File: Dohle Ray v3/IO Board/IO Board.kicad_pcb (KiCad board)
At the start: 2 copper layers, 50 x 41 mm, 5 parts, among them J1 Conn_01x07_Female, SW1 SW_SPDT

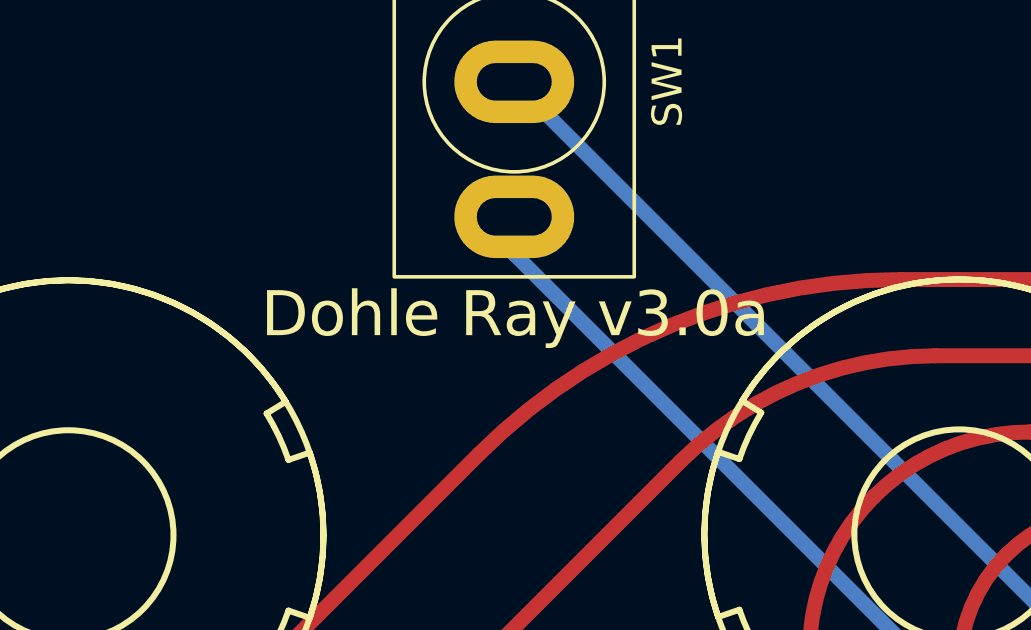
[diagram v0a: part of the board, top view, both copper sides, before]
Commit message: Update resistor values to have unity gain at 0% volume and gain knob, update PCB revision
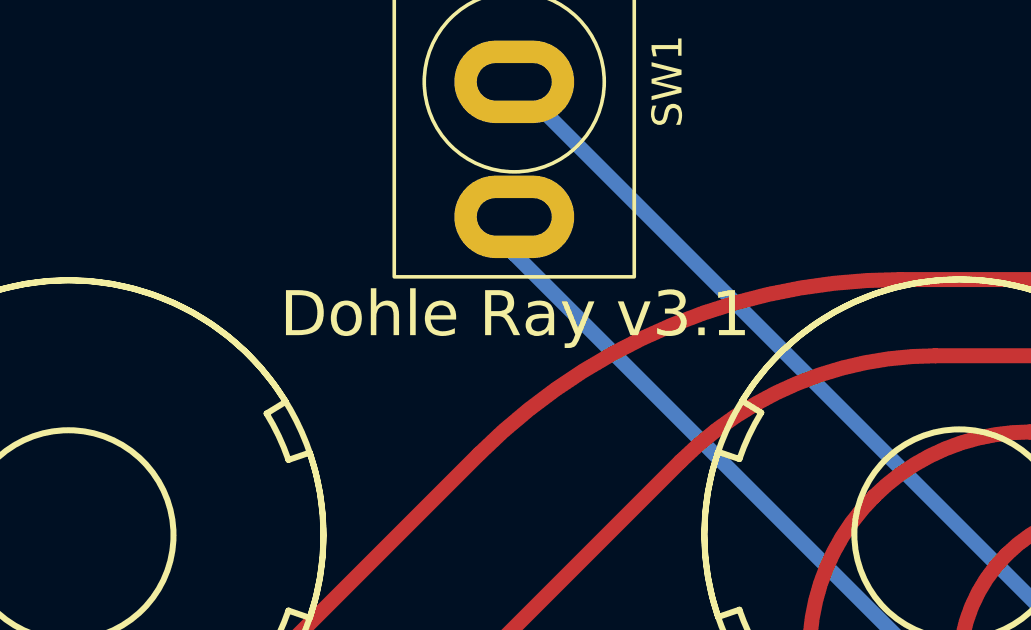
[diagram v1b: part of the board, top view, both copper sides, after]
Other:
- board text added: "Dohle Ray v3.1"
- board text removed: "Dohle Ray v3.0a"
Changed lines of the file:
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@@
   (gr_line (start 164.223286 135.963496) (end 164.223286 98.963496) (layer "Edge.Cuts") (width 0.2))
   (gr_line (start 162.223286 96.963496) (end 116.223286 96.963496) (layer "Edge.Cuts") (width 0.2))
-  (gr_text "Dohle Ray v3.0a" (at 139.2428 111.4044) (layer "F.SilkS")
+  (gr_text "Dohle Ray v3.1" (at 139.2428 111.4044) (layer "F.SilkS")
     (effects (font (size 1.5 1.5) (thickness 0.3)))
   )
